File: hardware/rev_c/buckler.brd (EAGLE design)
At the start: 63.5 x 114.3 mm, 91 parts, among them J1 DB25_5747846, J2 DM3AT-SF-PEJM5, J7 NRF52832DK_SHIELD, U1 ADXL327, U2 MAX44009, U3 MPU-9250, U4 MS5637-02BA03, U5 SI7021-A20-GM1, U6 SIP32510

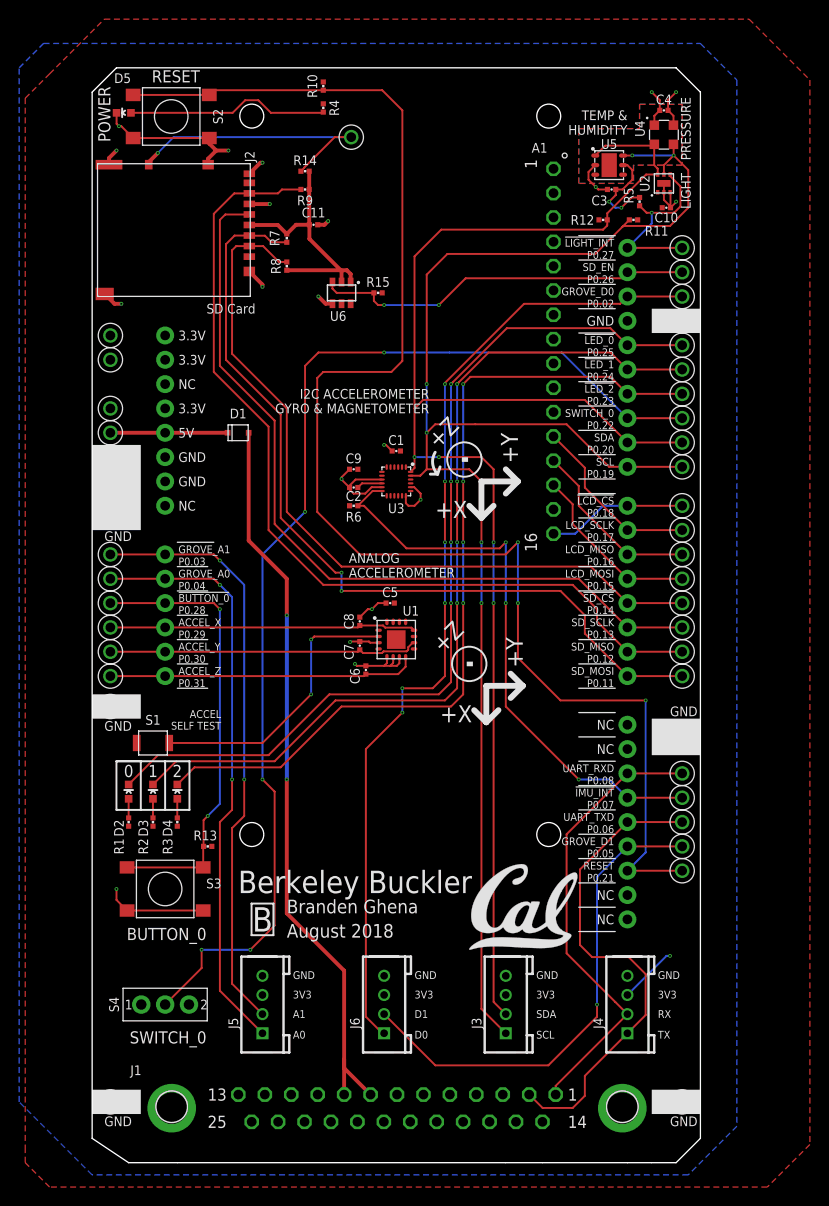
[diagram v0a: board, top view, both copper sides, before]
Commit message: Address problems in #2
Reroute light, temp/hum, pressure sensors to make room for IC number
labels. Rename 3v3->VCC. Flip UART RX/TX on DB25 connector. Move gyro
axis label out from under LCD screen.
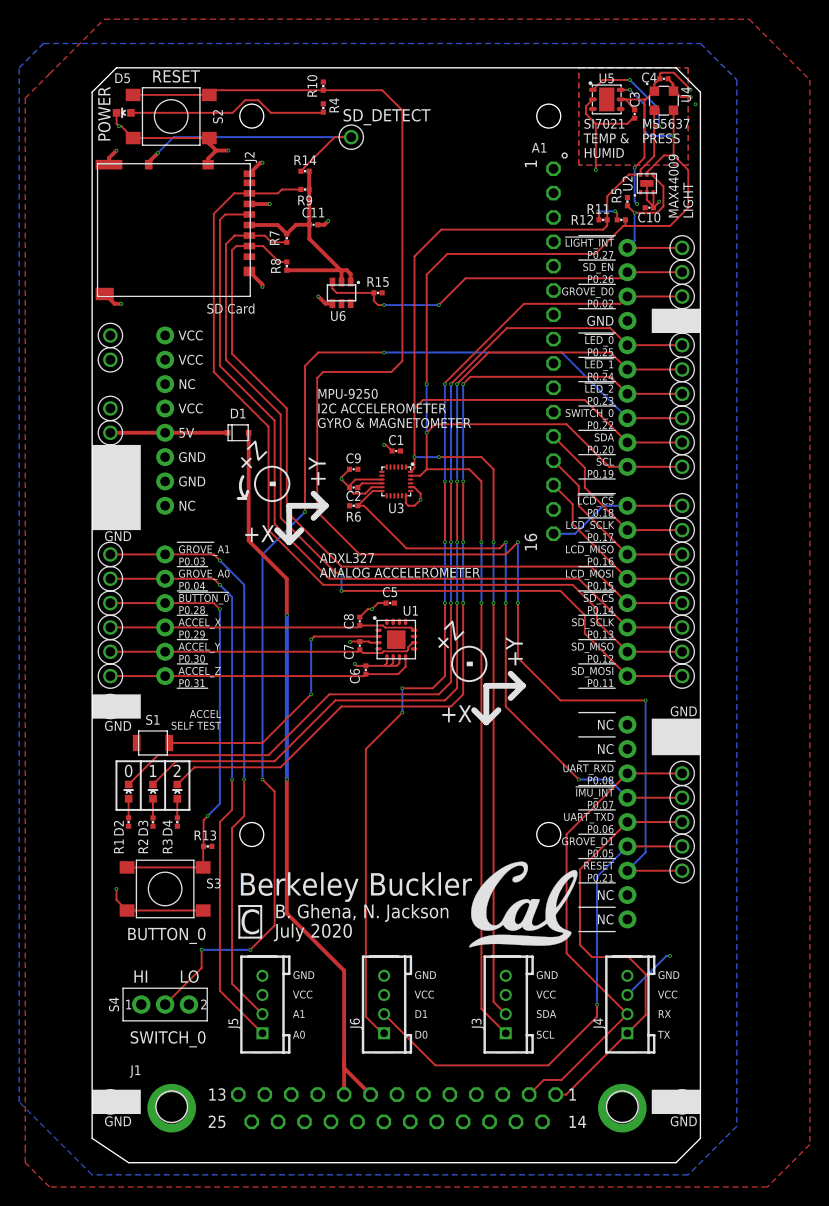
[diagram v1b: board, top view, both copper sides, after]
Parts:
- moved C3 8.24 mm to (56.6, 103.1), turned to 270 degrees
- moved U5 6.86 mm to (53.7, 104.6)
- moved U4 3.56 mm to (59.7, 104.5)
- moved C4 3.30 mm to (59.7, 106.8)
- moved C10 1.78 mm to (58.2, 93.3)
- moved U2 1.78 mm to (57.9, 95.9)
- moved R11 1.27 mm to (55.2, 92.1), turned to 180 degrees
- moved R5 1.27 mm to (55.9, 94.0)
- moved U$5 0.25 mm to (39.4, 16.1)
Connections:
- net UART_RX: now also J1.2; no longer J1.1
- net UART_TX: now also J1.1; no longer J1.2
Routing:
- net +3V3: track 19.9 -> 33.2 mm, vias 4 -> 6
- net GND: track 83.4 -> 92.6 mm, vias 19 -> 20
- net SENSORS_SCL: track 162.3 -> 170.6 mm, vias 6 -> 7
- net SENSORS_SDA: track 158.6 -> 166.1 mm, vias 4 -> 6
- net UART_TX: track 51.1 -> 45.9 mm
- net UART_RX: track 47.6 -> 49.8 mm
- net !LIGHT_INTERRUPT: track 19.1 -> 17.8 mm
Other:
- outline, holes or cut-outs redrawn
- board text added: "ADXL327 ANALOG ACCELEROMETER"
- board text added: "B. Ghena, N. Jackson"
- board text added: "C"
- board text added: "HI"
- board text added: "July 2020"
- board text added: "LO"
- board text added: "MAX44009 LIGHT"
- board text added: "MPU-9250 I2C ACCELEROMETER GYRO & MAGNETOMETER"
- board text added: "MS5637 PRESS"
- board text added: "SD_DETECT"
- board text added: "SI7021 TEMP & HUMID"
- board text added: "VCC"
- board text removed: "3V3"
- board text removed: "ANALOG ACCELEROMETER"
- board text removed: "August 2018"
- board text removed: "B"
- board text removed: "Branden Ghena"
- board text removed: "I2C ACCELEROMETER GYRO & MAGNETOMETER"
- board text removed: "LIGHT"
- board text removed: "PRESSURE"
- board text removed: "TEMP & HUMIDITY"
